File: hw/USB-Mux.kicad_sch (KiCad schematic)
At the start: 63 parts, among them J101 USB-61400416121, J102 USB-676432911, J103 USB-61400416121, J104 USB-676432911, Q101 DTC114EE, Q102 DTC114EE, Q103 DTC114EE, Q104 DTC114EE, U101 TS3USB3000, U102 TS3USB3000, U103 TPS22976, U104 TPS22976, U105 TUSB212, X101 Lightpipe-5x12.7mm-Dome, X102 Lightpipe-5x12.7mm-Dome, X103 Lightpipe-5x12.7mm-Dome, X104 Lightpipe-5x12.7mm-Dome, X105 Lightpipe-5x12.7mm-Dome

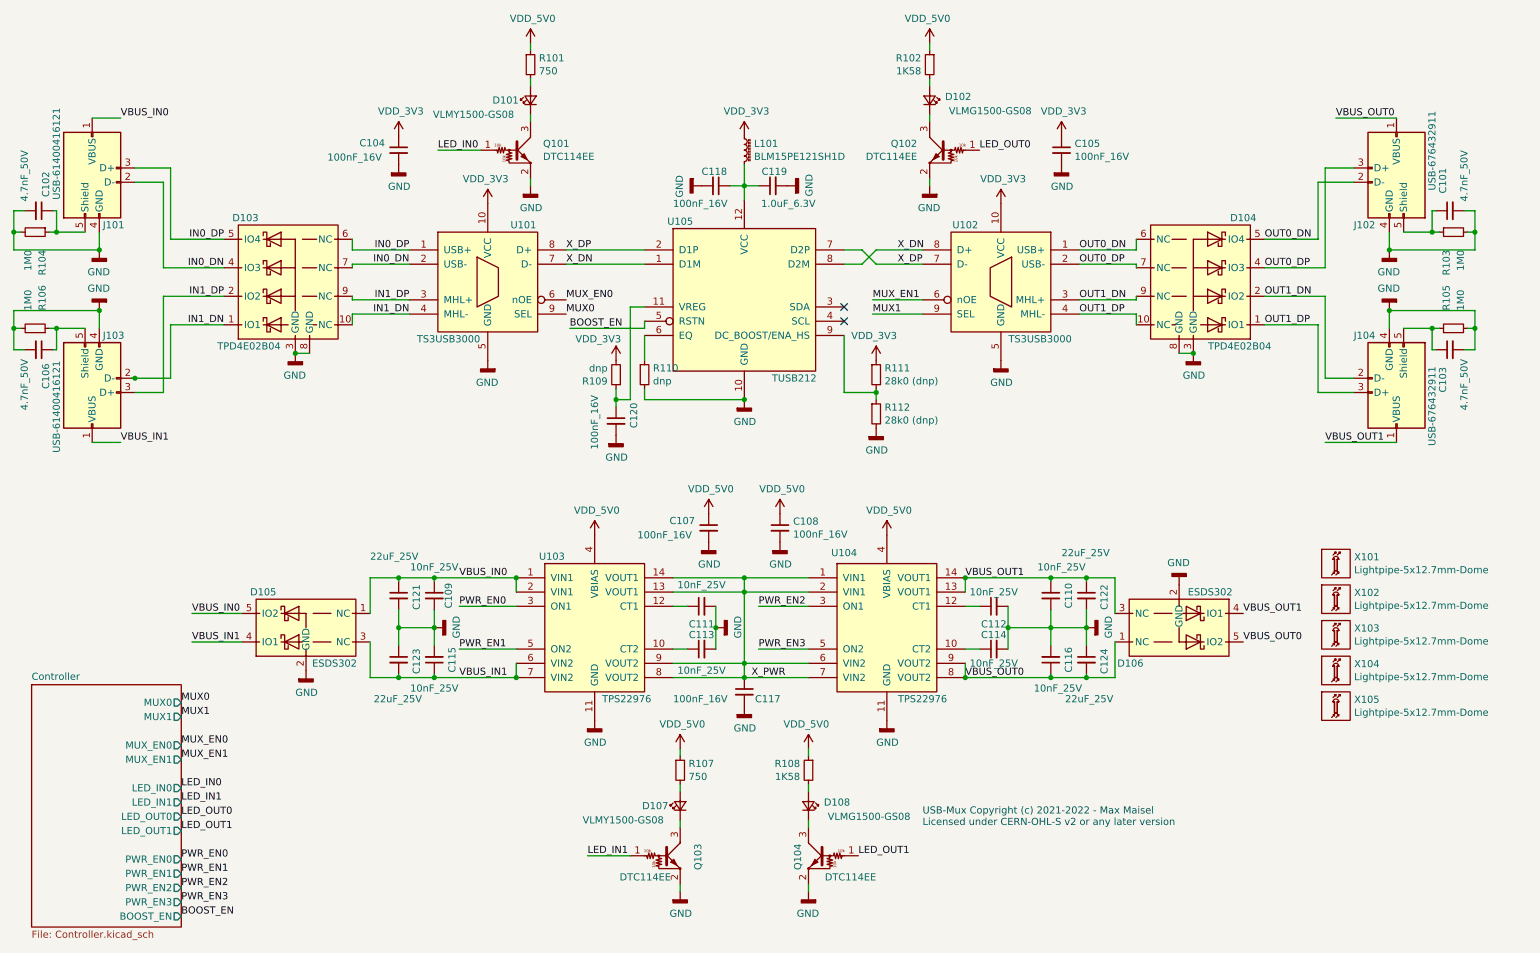
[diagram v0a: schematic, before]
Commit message: Cleanup Library
Remove unused ESD diode component and consistently name resistors X.XR.
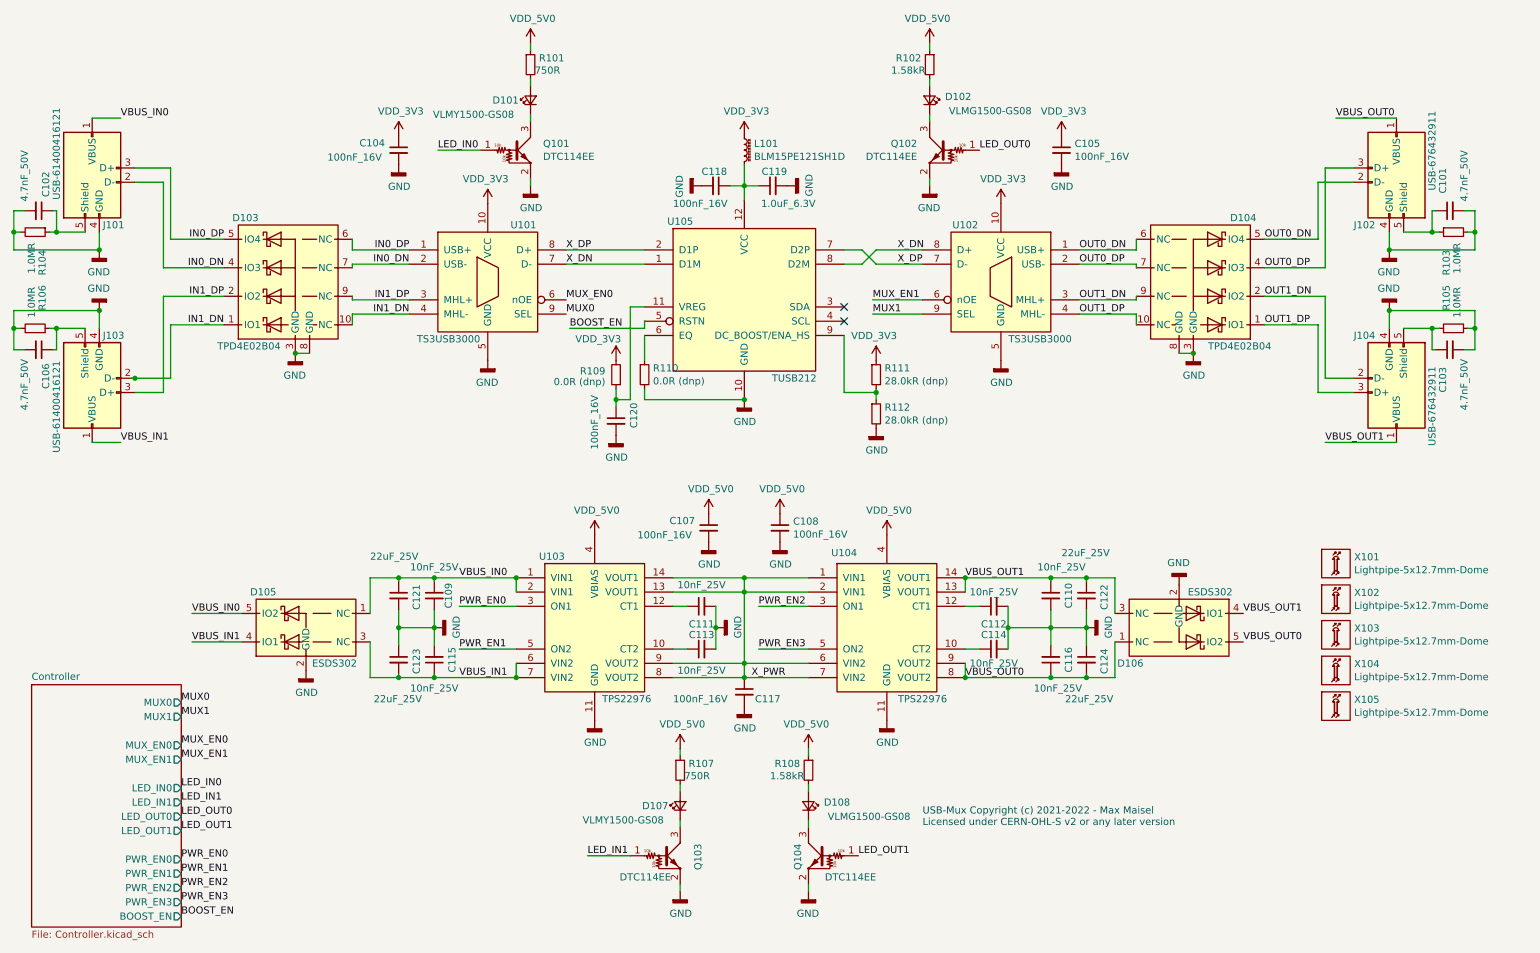
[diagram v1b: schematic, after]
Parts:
- R101, R107: value 750 -> 750R; symbol USB-Mux:750 -> USB-Mux:750R
- R102, R108: value 1K58 -> 1.58kR; symbol USB-Mux:1K58 -> USB-Mux:1.58kR
- R103, R104, R105, R106: value 1M0 -> 1.0MR; symbol USB-Mux:1M0 -> USB-Mux:1.0MR
- R109, R110: value dnp -> 0.0R (dnp); symbol USB-Mux:0R0 -> USB-Mux:0.0R
- R111, R112: value 28k0 (dnp) -> 28.0kR (dnp); symbol USB-Mux:28k0 -> USB-Mux:28.0kR
